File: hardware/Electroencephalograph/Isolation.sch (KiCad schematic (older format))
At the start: 14 parts, among them U4 THI3-0511, U5 ADUM2401BRWZ

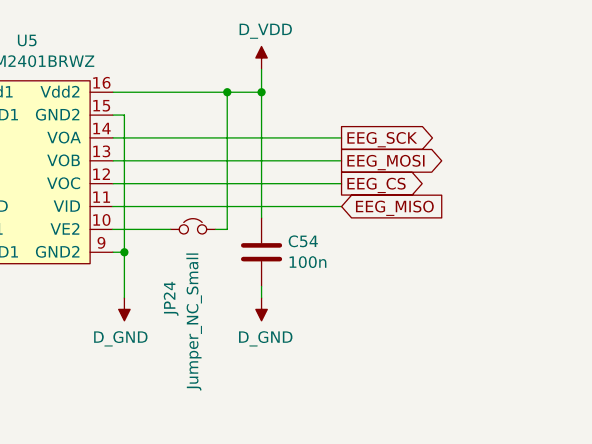
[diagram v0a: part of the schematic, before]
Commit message: fixed spi lines
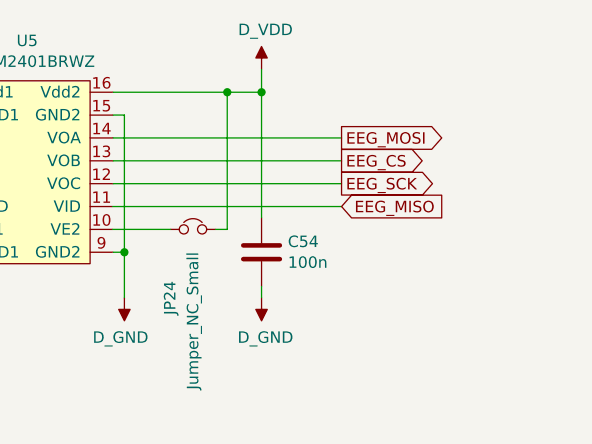
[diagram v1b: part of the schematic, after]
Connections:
- net EEG_CS: now also U5.13 (VOB); no longer U5.12 (VOC)
- net EEG_MOSI: now also U5.14 (VOA); no longer U5.13 (VOB)
- net EEG_SCK: now also U5.12 (VOC); no longer U5.14 (VOA)
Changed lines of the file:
@@
 	3950 2600 3950 3200
 Connection ~ 3950 3200
-Text GLabel 4900 2700 2    50   Output ~ 0
-EEG_SCK
-Text GLabel 4900 2800 2    50   Output ~ 0
-EEG_MOSI
-Text GLabel 4900 2900 2    50   Output ~ 0
-EEG_CS
 Text GLabel 4900 3000 2    50   Input ~ 0
 EEG_MISO
@@
 	1    0    0    -1
 $EndComp
+Text GLabel 4900 2900 2    50   Output ~ 0
+EEG_SCK
+Text GLabel 4900 2700 2    50   Output ~ 0
+EEG_MOSI
+Text GLabel 4900 2800 2    50   Output ~ 0
+EEG_CS
 $EndSCHEMATC

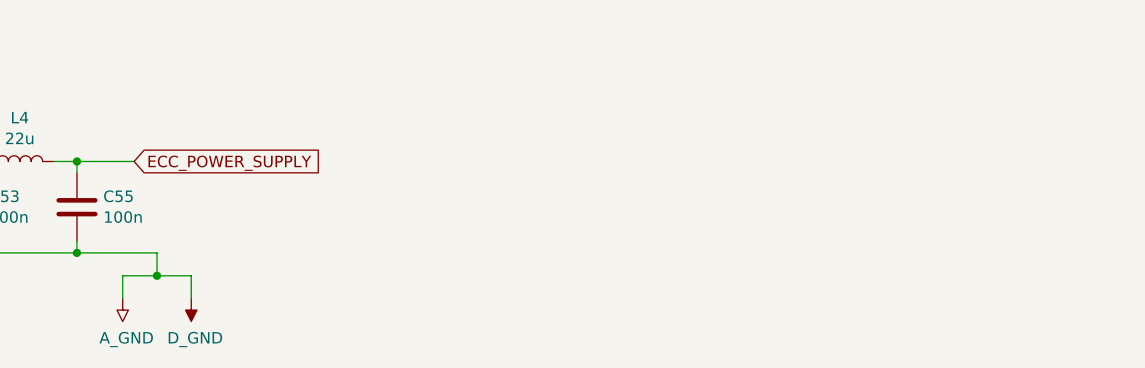
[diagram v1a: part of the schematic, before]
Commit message: split of analog and digital ground
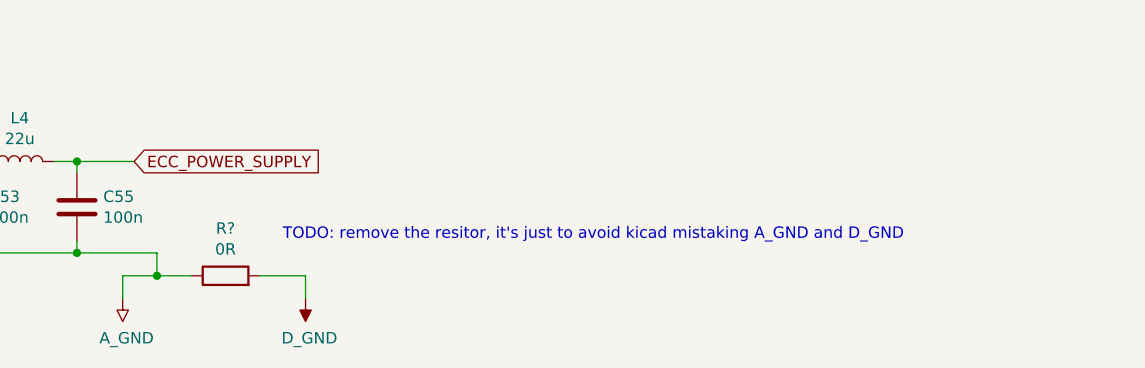
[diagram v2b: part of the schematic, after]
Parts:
- added R?: 0R, Resistor_SMD:R_0402_1005Metric, symbol Device:R
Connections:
- net A_GND: now also R?.1; no longer C54.2, U5.15 (GND2), U5.9 (GND2)
- new net D_GND: C54.2, R?.2, U5.15 (GND2), U5.9 (GND2)
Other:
- note added: "TODO: remove the resitor, it's just to avoid kicad mistaking A_GND and D_GND"
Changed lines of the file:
@@
 L Electroencephalograph:D_GND #PWR109
 U 1 1 5E03B5A4
-P 5200 5400
-F 0 "#PWR109" H 5200 5425 50  0001 C CNN
-F 1 "D_GND" H 5217 5227 50  0000 C CNN
-F 2 "" H 5200 5425 50  0001 C CNN
-F 3 "" H 5200 5425 50  0001 C CNN
-	1    5200 5400
+P 5700 5400
+F 0 "#PWR109" H 5700 5425 50  0001 C CNN
+F 1 "D_GND" H 5717 5227 50  0000 C CNN
+F 2 "" H 5700 5425 50  0001 C CNN
+F 3 "" H 5700 5425 50  0001 C CNN
+	1    5700 5400
 	1    0    0    -1
 $EndComp
@@
 	4900 5300 4900 5400
 Wire Wire Line
-	5200 5300 5200 5400
+	5700 5300 5700 5400
 Wire Wire Line
 	2800 5200 2650 5200
@@
 Wire Wire Line
 	4900 5300 5050 5300
-Connection ~ 5050 5300
-Wire Wire Line
-	5050 5300 5200 5300
 $Comp
 L Electroencephalograph:DP_GND #PWR177
@@
 Text GLabel 4900 2800 2    50   Output ~ 0
 EEG_CS
+$Comp
+L Device:R R?
+U 1 1 5E15FD88
+P 5350 5300
+AR Path="/5E15FD88" Ref="R?"  Part="1"
+AR Path="/5DF4CFF8/5E15FD88" Ref="R?"  Part="1"
+AR Path="/5DF61103/5E15FD88" Ref="R?"  Part="1"
+AR Path="/5DFE0AD6/5E15FD88" Ref="R?"  Part="1"
+F 0 "R?" V 5557 5300 50  0000 C CNN
+F 1 "0R" V 5466 5300 50  0000 C CNN
+F 2 "Resistor_SMD:R_0402_1005Metric" V 5280 5300 50  0001 C CNN
+F 3 "~" H 5350 5300 50  0001 C CNN
+	1    5350 5300
+	0    -1   -1   0
+$EndComp
+Wire Wire Line
+	5050 5300 5200 5300
+Connection ~ 5050 5300
+Wire Wire Line
+	5500 5300 5700 5300
+Text Notes 5600 5150 0    50   ~ 0
+TODO: remove the resitor, it's just to avoid kicad mistaking A_GND and D_GND
 $EndSCHEMATC

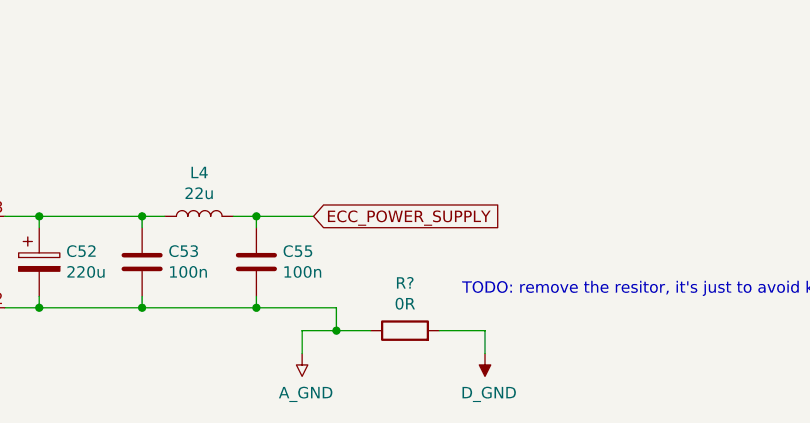
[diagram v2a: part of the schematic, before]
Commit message: added procesing unit
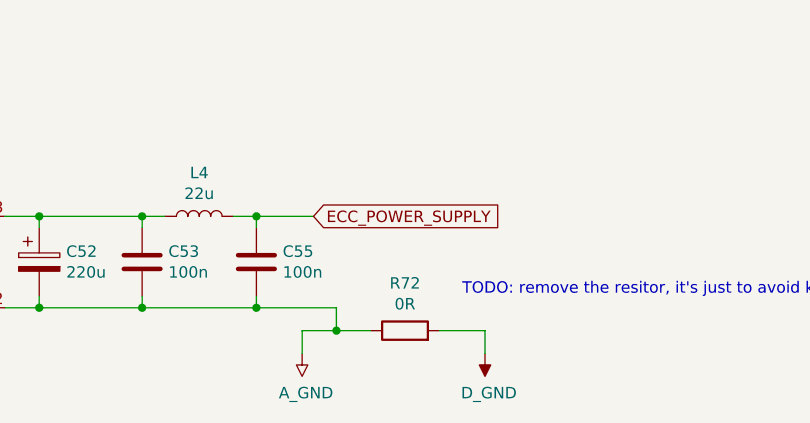
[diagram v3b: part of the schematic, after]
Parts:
- R72: renamed from R?; footprint Resistor_SMD:R_0402_1005Metric -> Resistor_SMD:R_0201_0603Metric
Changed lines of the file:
@@
 AR Path="/5DF4CFF8/5E15FD88" Ref="R?"  Part="1"
 AR Path="/5DF61103/5E15FD88" Ref="R?"  Part="1"
-AR Path="/5DFE0AD6/5E15FD88" Ref="R?"  Part="1"
-F 0 "R?" V 5557 5300 50  0000 C CNN
+AR Path="/5DFE0AD6/5E15FD88" Ref="R72"  Part="1"
+F 0 "R72" V 5557 5300 50  0000 C CNN
 F 1 "0R" V 5466 5300 50  0000 C CNN
-F 2 "Resistor_SMD:R_0402_1005Metric" V 5280 5300 50  0001 C CNN
+F 2 "Resistor_SMD:R_0201_0603Metric" V 5280 5300 50  0001 C CNN
 F 3 "~" H 5350 5300 50  0001 C CNN
 	1    5350 5300

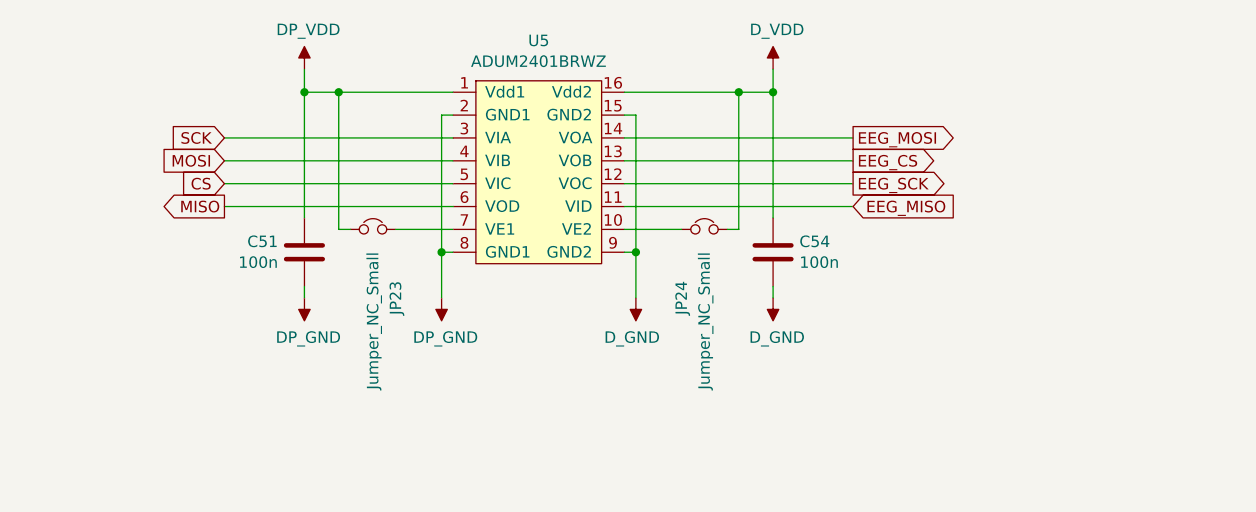
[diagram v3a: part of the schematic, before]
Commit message: routing of analog power supply
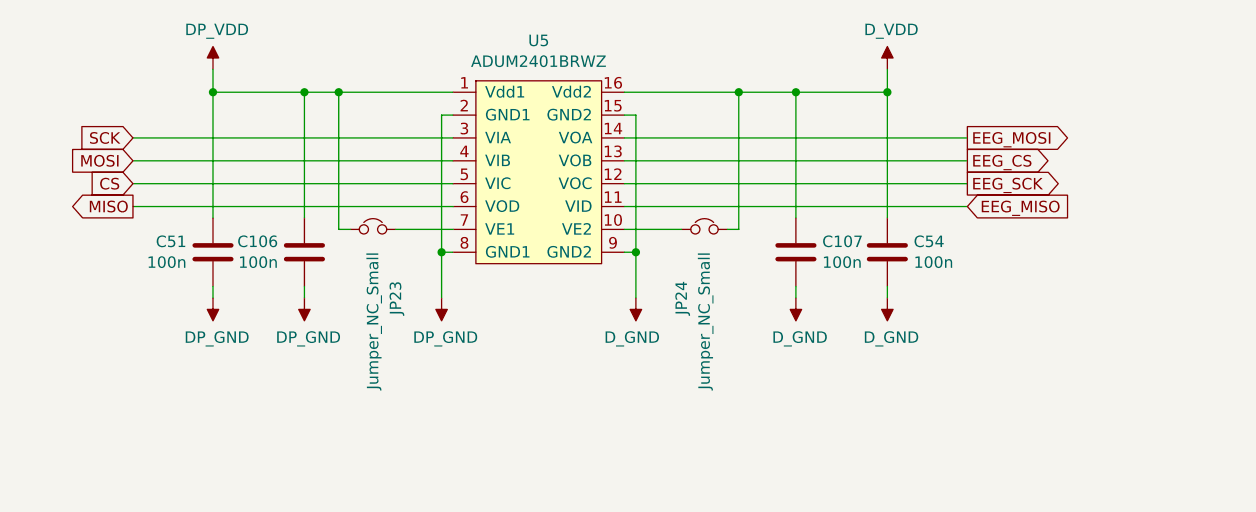
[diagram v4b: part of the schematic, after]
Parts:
- added C106, C107: 100n, Capacitor_SMD:C_0402_1005Metric, symbol Device:C
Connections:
- net DP_GND: now also C106.2
- net DP_VDD: now also C106.1
- net D_GND: now also C107.2
- net D_VDD: now also C107.1
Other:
- moved on the sheet: C51, C54
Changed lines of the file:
@@
 	3950 2600 3950 3200
 Connection ~ 3950 3200
-Text GLabel 4900 3000 2    50   Input ~ 0
+Text GLabel 5400 3000 2    50   Input ~ 0
 EEG_MISO
 Wire Wire Line
-	3900 2700 4900 2700
-Wire Wire Line
-	3900 2800 4900 2800
-Wire Wire Line
-	3900 2900 4900 2900
-Wire Wire Line
-	3900 3000 4900 3000
-Wire Wire Line
-	4550 3400 4550 3350
-Connection ~ 4550 2500
-Wire Wire Line
-	4550 2500 4550 2400
+	3900 2700 5400 2700
+Wire Wire Line
+	3900 2800 5400 2800
+Wire Wire Line
+	3900 2900 5400 2900
+Wire Wire Line
+	3900 3000 5400 3000
+Wire Wire Line
+	5050 3400 5050 3350
+Connection ~ 5050 2500
+Wire Wire Line
+	5050 2500 5050 2400
 $Comp
 L Electroencephalograph:D_VDD #PWR?
 U 1 1 5E000D6D
-P 4550 2400
+P 5050 2400
 AR Path="/5DF61103/5E000D6D" Ref="#PWR?"  Part="1"
 AR Path="/5DFE0AD6/5E000D6D" Ref="#PWR106"  Part="1"
-F 0 "#PWR106" H 4550 2525 50  0001 C CNN
-F 1 "D_VDD" H 4567 2573 50  0000 C CNN
-F 2 "" H 4550 2525 50  0001 C CNN
-F 3 "" H 4550 2525 50  0001 C CNN
-	1    4550 2400
+F 0 "#PWR106" H 5050 2525 50  0001 C CNN
+F 1 "D_VDD" H 5067 2573 50  0000 C CNN
+F 2 "" H 5050 2525 50  0001 C CNN
+F 3 "" H 5050 2525 50  0001 C CNN
+	1    5050 2400
 	1    0    0    -1
 $EndComp
@@
 L Electroencephalograph:D_GND #PWR?
 U 1 1 5E000D67
-P 4550 3400
+P 5050 3400
 AR Path="/5DF61103/5E000D67" Ref="#PWR?"  Part="1"
 AR Path="/5DFE0AD6/5E000D67" Ref="#PWR107"  Part="1"
-F 0 "#PWR107" H 4550 3425 50  0001 C CNN
-F 1 "D_GND" H 4567 3227 50  0000 C CNN
-F 2 "" H 4550 3425 50  0001 C CNN
-F 3 "" H 4550 3425 50  0001 C CNN
-	1    4550 3400
-	1    0    0    -1
-$EndComp
-Wire Wire Line
-	4550 2500 4550 3050
+F 0 "#PWR107" H 5050 3425 50  0001 C CNN
+F 1 "D_GND" H 5067 3227 50  0000 C CNN
+F 2 "" H 5050 3425 50  0001 C CNN
+F 3 "" H 5050 3425 50  0001 C CNN
+	1    5050 3400
+	1    0    0    -1
+$EndComp
+Wire Wire Line
+	5050 2500 5050 3050
 $Comp
 L Device:C C?
 U 1 1 5E000D60
-P 4550 3200
+P 5050 3200
 AR Path="/5DF4CFF8/5E000D60" Ref="C?"  Part="1"
 AR Path="/5DF61103/5E000D60" Ref="C?"  Part="1"
 AR Path="/5DFE0AD6/5E000D60" Ref="C54"  Part="1"
-F 0 "C54" H 4665 3246 50  0000 L CNN
-F 1 "100n" H 4665 3155 50  0000 L CNN
-F 2 "Capacitor_SMD:C_0402_1005Metric" H 4588 3050 50  0001 C CNN
-F 3 "~" H 4550 3200 50  0001 C CNN
-	1    4550 3200
+F 0 "C54" H 5165 3246 50  0000 L CNN
+F 1 "100n" H 5165 3155 50  0000 L CNN
+F 2 "Capacitor_SMD:C_0402_1005Metric" H 5088 3050 50  0001 C CNN
+F 3 "~" H 5050 3200 50  0001 C CNN
+	1    5050 3200
 	1    0    0    -1
 $EndComp
@@
 Connection ~ 4400 2500
 Wire Wire Line
-	4400 2500 4550 2500
+	4400 2500 4650 2500
 Wire Wire Line
 	3150 3200 3100 3200
@@
 Wire Wire Line
 	3100 2600 3100 3200
-Text GLabel 2150 2700 0    50   Input ~ 0
+Text GLabel 1750 2700 0    50   Input ~ 0
 SCK
-Text GLabel 2150 2800 0    50   Input ~ 0
+Text GLabel 1750 2800 0    50   Input ~ 0
 MOSI
-Text GLabel 2150 2900 0    50   Input ~ 0
+Text GLabel 1750 2900 0    50   Input ~ 0
 CS
-Text GLabel 2150 3000 0    50   Output ~ 0
+Text GLabel 1750 3000 0    50   Output ~ 0
 MISO
 Wire Wire Line
-	3150 2700 2150 2700
-Wire Wire Line
-	3150 2800 2150 2800
-Wire Wire Line
-	3150 2900 2150 2900
-Wire Wire Line
-	3150 3000 2150 3000
-Connection ~ 2500 2500
-Wire Wire Line
-	2500 2500 2500 2400
-Wire Wire Line
-	2500 2500 2500 3050
+	3150 2700 1750 2700
+Wire Wire Line
+	3150 2800 1750 2800
+Wire Wire Line
+	3150 2900 1750 2900
+Wire Wire Line
+	3150 3000 1750 3000
+Connection ~ 2100 2500
+Wire Wire Line
+	2100 2500 2100 2400
+Wire Wire Line
+	2100 2500 2100 3050
 $Comp
 L Device:C C?
 U 1 1 5E028BA8
-P 2500 3200
+P 2100 3200
 AR Path="/5DF4CFF8/5E028BA8" Ref="C?"  Part="1"
 AR Path="/5DF61103/5E028BA8" Ref="C?"  Part="1"
 AR Path="/5DFE0AD6/5E028BA8" Ref="C51"  Part="1"
-F 0 "C51" H 2615 3246 50  0000 L CNN
-F 1 "100n" H 2615 3155 50  0000 L CNN
-F 2 "Capacitor_SMD:C_0402_1005Metric" H 2538 3050 50  0001 C CNN
-F 3 "~" H 2500 3200 50  0001 C CNN
-	1    2500 3200
+F 0 "C51" H 2215 3246 50  0000 L CNN
+F 1 "100n" H 2215 3155 50  0000 L CNN
+F 2 "Capacitor_SMD:C_0402_1005Metric" H 2138 3050 50  0001 C CNN
+F 3 "~" H 2100 3200 50  0001 C CNN
+	1    2100 3200
 	-1   0    0    -1
 $EndComp
@@
 	2650 3100 2650 2500
 Connection ~ 2650 2500
-Wire Wire Line
-	2650 2500 2500 2500
 $Comp
 L Device:C C?
@@
 L Electroencephalograph:DP_VDD #PWR101
 U 1 1 5E02F433
-P 2500 2400
-F 0 "#PWR101" H 2500 2525 50  0001 C CNN
-F 1 "DP_VDD" H 2517 2573 50  0000 C CNN
-F 2 "" H 2500 2525 50  0001 C CNN
-F 3 "" H 2500 2525 50  0001 C CNN
-	1    2500 2400
+P 2100 2400
+F 0 "#PWR101" H 2100 2525 50  0001 C CNN
+F 1 "DP_VDD" H 2117 2573 50  0000 C CNN
+F 2 "" H 2100 2525 50  0001 C CNN
+F 3 "" H 2100 2525 50  0001 C CNN
+	1    2100 2400
 	1    0    0    -1
 $EndComp
@@
 L Electroencephalograph:DP_GND #PWR102
 U 1 1 5E02EFAB
-P 2500 3400
-F 0 "#PWR102" H 2500 3425 50  0001 C CNN
-F 1 "DP_GND" H 2517 3227 50  0000 C CNN
-F 2 "" H 2500 3425 50  0001 C CNN
-F 3 "" H 2500 3425 50  0001 C CNN
-	1    2500 3400
+P 2100 3400
+F 0 "#PWR102" H 2100 3425 50  0001 C CNN
+F 1 "DP_GND" H 2117 3227 50  0000 C CNN
+F 2 "" H 2100 3425 50  0001 C CNN
+F 3 "" H 2100 3425 50  0001 C CNN
+	1    2100 3400
 	1    0    0    -1
 $EndComp
@@
 $EndComp
 Wire Wire Line
-	2500 3400 2500 3350
+	2100 3400 2100 3350
 Connection ~ 3100 3200
 Wire Wire Line
@@
 	1    0    0    -1
 $EndComp
-Text GLabel 4900 2900 2    50   Output ~ 0
+Text GLabel 5400 2900 2    50   Output ~ 0
 EEG_SCK
-Text GLabel 4900 2700 2    50   Output ~ 0
+Text GLabel 5400 2700 2    50   Output ~ 0
 EEG_MOSI
-Text GLabel 4900 2800 2    50   Output ~ 0
+Text GLabel 5400 2800 2    50   Output ~ 0
 EEG_CS
 $Comp
@@
 Text Notes 5600 5150 0    50   ~ 0
 TODO: remove the resitor, it's just to avoid kicad mistaking A_GND and D_GND
+$Comp
+L Device:C C?
+U 1 1 5E203FB6
+P 2500 3200
+AR Path="/5DF4CFF8/5E203FB6" Ref="C?"  Part="1"
+AR Path="/5DF61103/5E203FB6" Ref="C?"  Part="1"
+AR Path="/5DFE0AD6/5E203FB6" Ref="C106"  Part="1"
+F 0 "C106" H 2615 3246 50  0000 L CNN
+F 1 "100n" H 2615 3155 50  0000 L CNN
+F 2 "Capacitor_SMD:C_0402_1005Metric" H 2538 3050 50  0001 C CNN
+F 3 "~" H 2500 3200 50  0001 C CNN
+	1    2500 3200
+	-1   0    0    -1
+$EndComp
+$Comp
+L Electroencephalograph:DP_GND #PWR193
+U 1 1 5E203FBC
+P 2500 3400
+F 0 "#PWR193" H 2500 3425 50  0001 C CNN
+F 1 "DP_GND" H 2517 3227 50  0000 C CNN
+F 2 "" H 2500 3425 50  0001 C CNN
+F 3 "" H 2500 3425 50  0001 C CNN
+	1    2500 3400
+	1    0    0    -1
+$EndComp
+Wire Wire Line
+	2500 3400 2500 3350
+Wire Wire Line
+	2500 3050 2500 2500
+Wire Wire Line
+	2100 2500 2500 2500
+Connection ~ 2500 2500
+Wire Wire Line
+	2500 2500 2650 2500
+Wire Wire Line
+	4650 3400 4650 3350
+$Comp
+L Electroencephalograph:D_GND #PWR?
+U 1 1 5E20CF7F
+P 4650 3400
+AR Path="/5DF61103/5E20CF7F" Ref="#PWR?"  Part="1"
+AR Path="/5DFE0AD6/5E20CF7F" Ref="#PWR194"  Part="1"
+F 0 "#PWR194" H 4650 3425 50  0001 C CNN
+F 1 "D_GND" H 4667 3227 50  0000 C CNN
+F 2 "" H 4650 3425 50  0001 C CNN
+F 3 "" H 4650 3425 50  0001 C CNN
+	1    4650 3400
+	1    0    0    -1
+$EndComp
+$Comp
+L Device:C C?
+U 1 1 5E20CF85
+P 4650 3200
+AR Path="/5DF4CFF8/5E20CF85" Ref="C?"  Part="1"
+AR Path="/5DF61103/5E20CF85" Ref="C?"  Part="1"
+AR Path="/5DFE0AD6/5E20CF85" Ref="C107"  Part="1"
+F 0 "C107" H 4765 3246 50  0000 L CNN
+F 1 "100n" H 4765 3155 50  0000 L CNN
+F 2 "Capacitor_SMD:C_0402_1005Metric" H 4688 3050 50  0001 C CNN
+F 3 "~" H 4650 3200 50  0001 C CNN
+	1    4650 3200
+	1    0    0    -1
+$EndComp
+Wire Wire Line
+	4650 3050 4650 2500
+Connection ~ 4650 2500
+Wire Wire Line
+	4650 2500 5050 2500
 $EndSCHEMATC
